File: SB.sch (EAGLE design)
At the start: 47 parts, among them IC1 ATMEGA32U4NT-TQFP, IC2 HX711-SOP16L, J1 RJ10-WURTH, J2 AUDIO-JACK-PJ321, J3 USB-C-16P-16P, K1 HE721C-DIP, Q1 2N7002, Q2 2N3906, SW1 SWITCH-SPDT-4TABSSMT, SW2 SWITCH-SPDT-4TABSSMT, SW3 RESET, SW4 Trigger Level, SW5 Tare

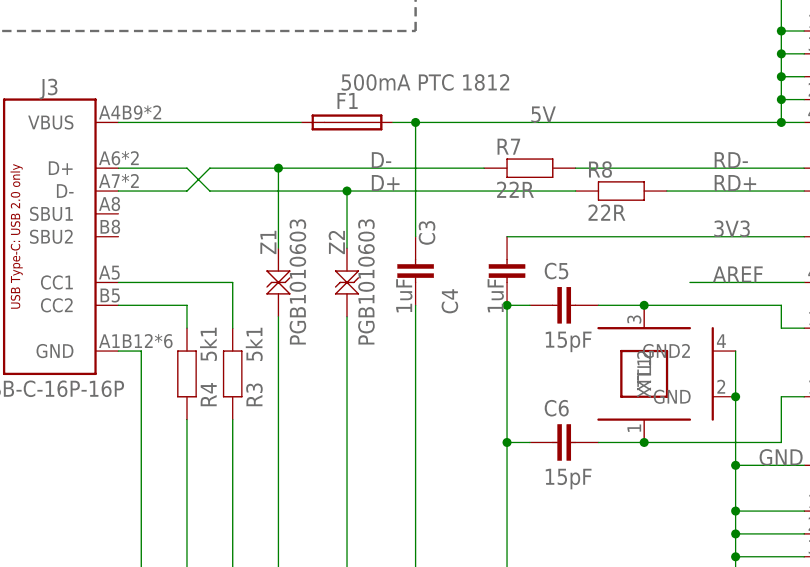
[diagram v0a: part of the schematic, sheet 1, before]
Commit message: Replaced capacitors to simplify BOM for production
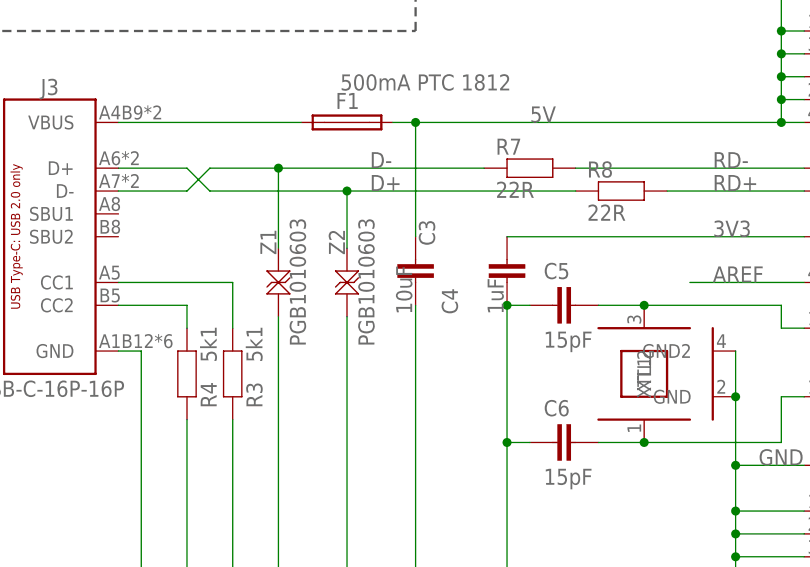
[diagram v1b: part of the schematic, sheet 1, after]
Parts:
- C10, C12: device SuperHouse-DiscreteSemi:CAP0603 -> SuperHouse-DiscreteSemi:CAP0805
- C3: value 1uF -> 10uF
- C4: device SuperHouse-DiscreteSemi:CAP0805 -> SuperHouse-DiscreteSemi:CAP0603
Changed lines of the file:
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@@
 <?xml version="1.0" encoding="utf-8"?>
 <!DOCTYPE eagle SYSTEM "eagle.dtd">
-<eagle version="9.6.1">
+<eagle version="9.6.2">
 <drawing>
 <settings>
@@
 <part name="R5" library="SuperHouse-DiscreteSemi" library_urn="urn:adsk.eagle:library:11768461" deviceset="RESISTOR" device="0603" package3d_urn="urn:adsk.eagle:package:11768543/2" value="10K"/>
 <part name="U$1" library="SuperHouse-SupplySymbols" library_urn="urn:adsk.eagle:library:11790503" deviceset="5V" device=""/>
-<part name="C3" library="SuperHouse-DiscreteSemi" library_urn="urn:adsk.eagle:library:11768461" deviceset="CAP" device="0805" package3d_urn="urn:adsk.eagle:package:7066318/4" value="1uF"/>
+<part name="C3" library="SuperHouse-DiscreteSemi" library_urn="urn:adsk.eagle:library:11768461" deviceset="CAP" device="0805" package3d_urn="urn:adsk.eagle:package:7066318/4" value="10uF"/>
 <part name="C1" library="SuperHouse-DiscreteSemi" library_urn="urn:adsk.eagle:library:11768461" deviceset="CAP" device="0603" package3d_urn="urn:adsk.eagle:package:7066315/6" value="100nF"/>
 <part name="GND11" library="SuperHouse-SupplySymbols" library_urn="urn:adsk.eagle:library:11790503" deviceset="GND" device=""/>
@@
 <part name="C5" library="SuperHouse-DiscreteSemi" library_urn="urn:adsk.eagle:library:11768461" deviceset="CAP" device="0603" package3d_urn="urn:adsk.eagle:package:7066315/6" value="15pF"/>
 <part name="C6" library="SuperHouse-DiscreteSemi" library_urn="urn:adsk.eagle:library:11768461" deviceset="CAP" device="0603" package3d_urn="urn:adsk.eagle:package:7066315/6" value="15pF"/>
-<part name="C4" library="SuperHouse-DiscreteSemi" library_urn="urn:adsk.eagle:library:11768461" deviceset="CAP" device="0805" package3d_urn="urn:adsk.eagle:package:7066318/4" value="1uF"/>
+<part name="C4" library="SuperHouse-DiscreteSemi" library_urn="urn:adsk.eagle:library:11768461" deviceset="CAP" device="0603" package3d_urn="urn:adsk.eagle:package:7066315/6" value="1uF"/>
 <part name="XTL1" library="SuperHouse-Oscillators" library_urn="urn:adsk.eagle:library:11786724" deviceset="CRYSTAL-GND" device="3X2" package3d_urn="urn:adsk.eagle:package:7066259/2" value="16MHz"/>
 <part name="GND13" library="SuperHouse-SupplySymbols" library_urn="urn:adsk.eagle:library:11790503" deviceset="GND" device=""/>
@@
 <part name="R14" library="SuperHouse-DiscreteSemi" library_urn="urn:adsk.eagle:library:11768461" deviceset="RESISTOR" device="0603" package3d_urn="urn:adsk.eagle:package:11768543/2" value="8K2"/>
 <part name="L1" library="SuperHouse-DiscreteSemi" library_urn="urn:adsk.eagle:library:11768461" deviceset="INDUCTOR" device="0603" package3d_urn="urn:adsk.eagle:package:11872694/3" value="3.3uH"/>
-<part name="C10" library="SuperHouse-DiscreteSemi" library_urn="urn:adsk.eagle:library:11768461" deviceset="CAP" device="0603" package3d_urn="urn:adsk.eagle:package:7066315/6" value="10uF"/>
+<part name="C10" library="SuperHouse-DiscreteSemi" library_urn="urn:adsk.eagle:library:11768461" deviceset="CAP" device="0805" package3d_urn="urn:adsk.eagle:package:7066318/4" value="10uF"/>
 <part name="C11" library="SuperHouse-DiscreteSemi" library_urn="urn:adsk.eagle:library:11768461" deviceset="CAP" device="0603" package3d_urn="urn:adsk.eagle:package:7066315/6" value="100nF"/>
-<part name="C12" library="SuperHouse-DiscreteSemi" library_urn="urn:adsk.eagle:library:11768461" deviceset="CAP" device="0603" package3d_urn="urn:adsk.eagle:package:7066315/6" value="10uF"/>
+<part name="C12" library="SuperHouse-DiscreteSemi" library_urn="urn:adsk.eagle:library:11768461" deviceset="CAP" device="0805" package3d_urn="urn:adsk.eagle:package:7066318/4" value="10uF"/>
 <part name="SW1" library="SuperHouse-Switches" library_urn="urn:adsk.eagle:library:11744182" deviceset="SWITCH-SPDT-4TABS" device="SMT" package3d_urn="urn:adsk.eagle:package:7066359/2"/>
 <part name="GND10" library="SuperHouse-SupplySymbols" library_urn="urn:adsk.eagle:library:11790503" deviceset="GND" device=""/>
